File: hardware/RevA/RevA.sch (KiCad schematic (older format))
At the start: 143 parts, among them J1 USB_C_Receptacle_USB2.0, J2 DNP Conn_02x02_Odd_Even, J3 DNP Conn_01x02, J4 DNP Conn_02x03_Odd_Even, J5 DNP Conn_01x02, SW1 SW_Push, SW2 SW_Push, U1 SY8120B1ABC, U10 SPI RAM LY68L6400SLIT, U2 XC6206P25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

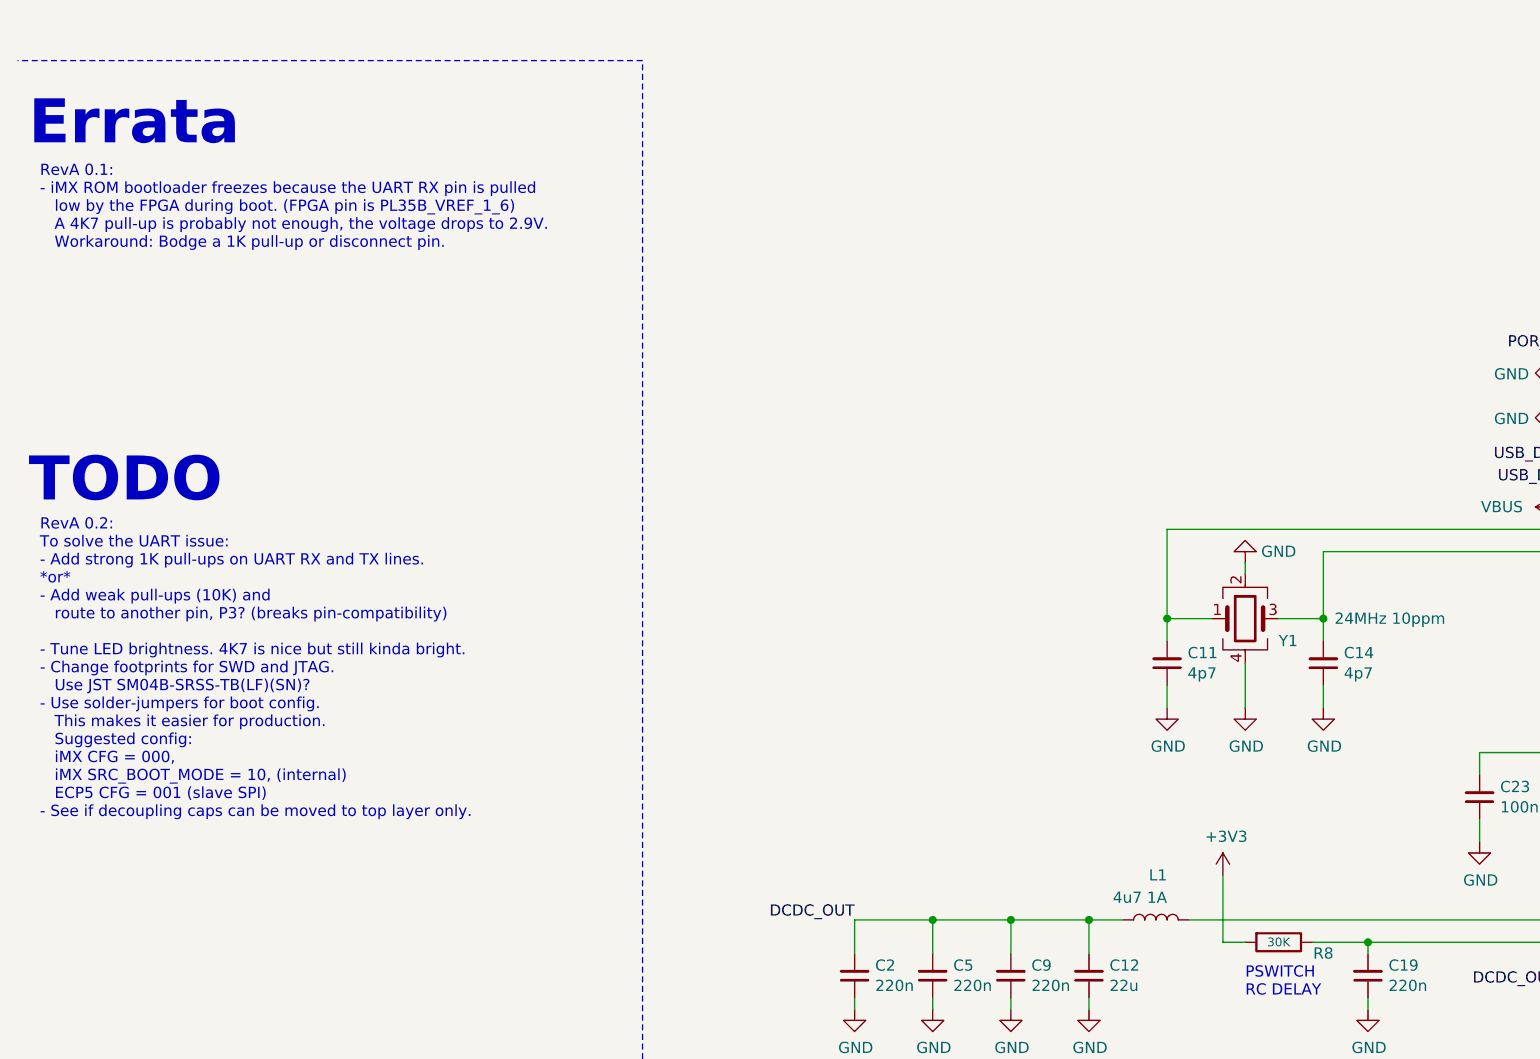
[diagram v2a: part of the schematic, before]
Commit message: Changed xtal load caps to 20pF
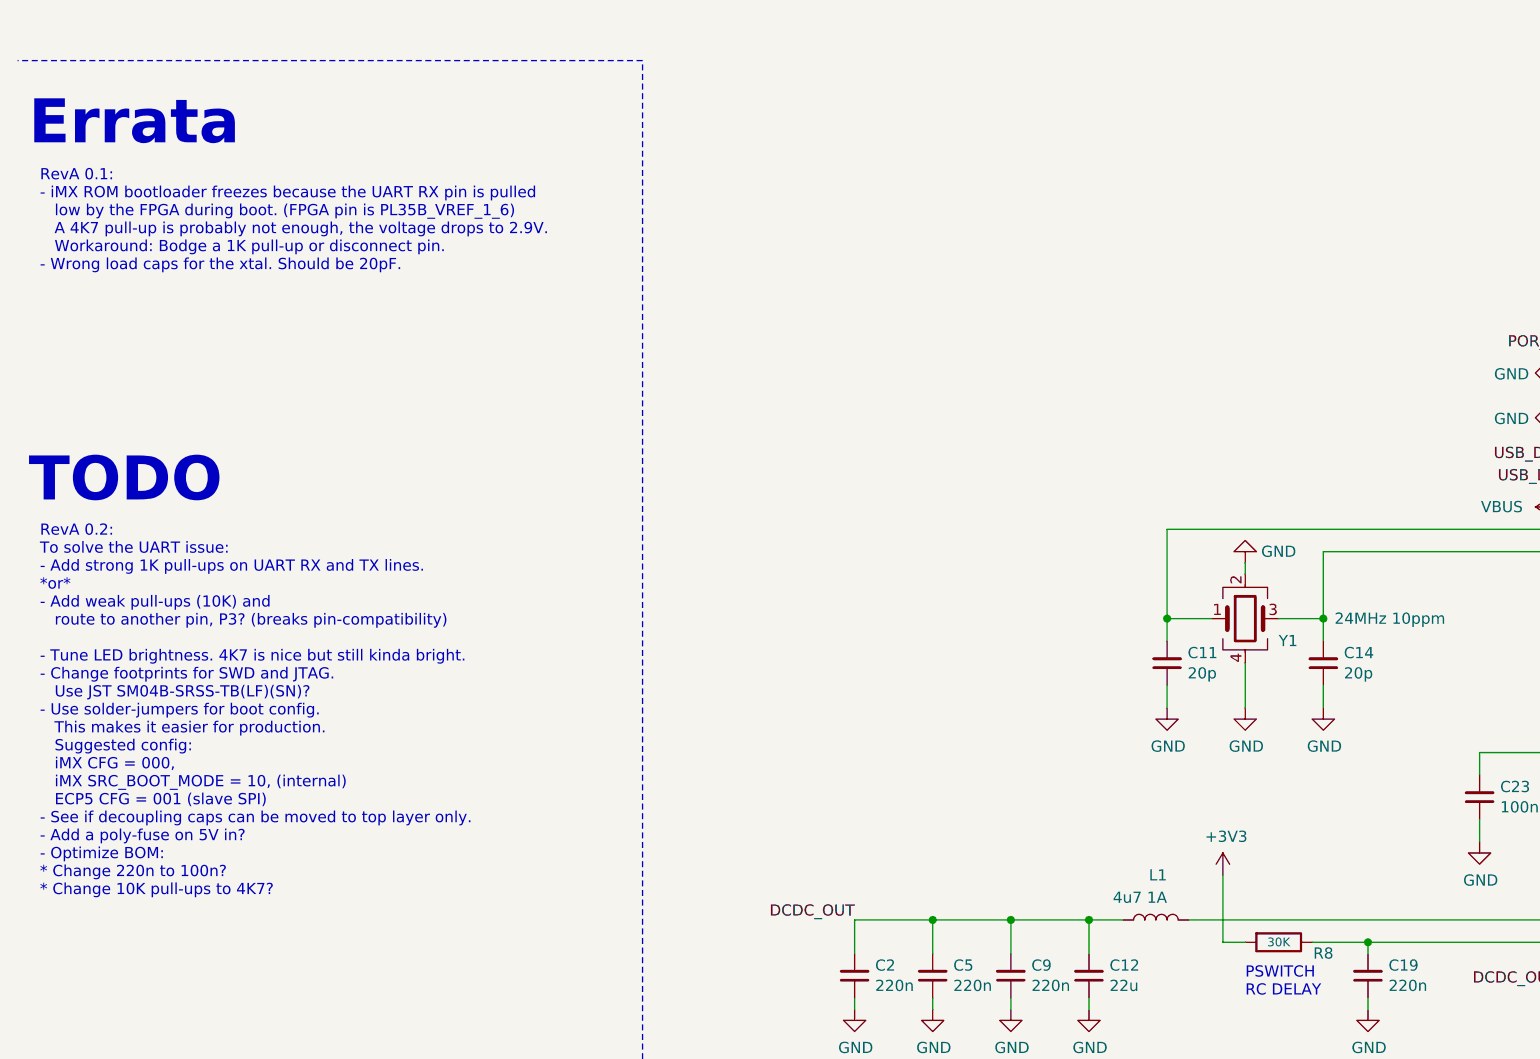
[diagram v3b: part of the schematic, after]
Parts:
- C11, C14: value 4p7 -> 20p
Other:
- note added: "RevA 0.1:\n- iMX ROM bootloader freezes because the UART RX pin is pulled\n low by the FPGA during boot. (FPGA pin is PL35B_VREF_1_6)\n A 4K7 pull-up is probably not enough, the voltage drops to 2.9V.\n Workaround: Bodge a 1K pull-up or disconnect pin.\n- Wrong load caps for the xtal. Should be 20pF."
- note removed: "RevA 0.1:\n- iMX ROM bootloader freezes because the UART RX pin is pulled\n low by the FPGA during boot. (FPGA pin is PL35B_VREF_1_6)\n A 4K7 pull-up is probably not enough, the voltage drops to 2.9V.\n Workaround: Bodge a 1K pull-up or disconnect pin.\n"
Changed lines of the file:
@@
 P 5700 12900
 F 0 "C11" H 5608 12854 50  0000 R CNN
-F 1 "4p7" H 5608 12945 50  0000 R CNN
+F 1 "20p" H 5608 12945 50  0000 R CNN
 F 2 "Capacitor_SMD:C_0402_1005Metric" H 5700 12900 50  0001 C CNN
 F 3 " " H 5700 12900 50  0001 C CNN
@@
 P 6400 12900
 F 0 "C14" H 6308 12854 50  0000 R CNN
-F 1 "4p7" H 6308 12945 50  0000 R CNN
+F 1 "20p" H 6308 12945 50  0000 R CNN
 F 2 "Capacitor_SMD:C_0402_1005Metric" H 6400 12900 50  0001 C CNN
 F 3 " " H 6400 12900 50  0001 C CNN
@@
 Text Notes 600  10600 0    197  ~ 39
 Errata
-Text Notes 650  11050 0    50   ~ 0
-RevA 0.1:\n- iMX ROM bootloader freezes because the UART RX pin is pulled\n   low by the FPGA during boot. (FPGA pin is PL35B_VREF_1_6)\n   A 4K7 pull-up is probably not enough, the voltage drops to 2.9V.\n   Workaround: Bodge a 1K pull-up or disconnect pin.\n
+Text Notes 650  11150 0    50   ~ 0
+RevA 0.1:\n- iMX ROM bootloader freezes because the UART RX pin is pulled\n   low by the FPGA during boot. (FPGA pin is PL35B_VREF_1_6)\n   A 4K7 pull-up is probably not enough, the voltage drops to 2.9V.\n   Workaround: Bodge a 1K pull-up or disconnect pin.\n- Wrong load caps for the xtal. Should be 20pF.
 Text Notes 600  12200 0    197  ~ 39
 TODO
-Text Notes 650  13600 0    50   ~ 0
-RevA 0.2:\nTo solve the UART issue:\n- Add strong 1K pull-ups on UART RX and TX lines.\n*or*\n- Add weak pull-ups (10K) and\n   route to another pin, P3? (breaks pin-compatibility)\n\n- Tune LED brightness. 4K7 is nice but still kinda bright.\n- Change footprints for SWD and JTAG.\n   Use JST SM04B-SRSS-TB(LF)(SN)?\n- Use solder-jumpers for boot config.\n   This makes it easier for production.\n   Suggested config:\n   iMX CFG = 000,\n   iMX SRC_BOOT_MODE = 10, (internal)\n   ECP5 CFG = 001 (slave SPI)\n- See if decoupling caps can be moved to top layer only.
+Text Notes 650  13950 0    50   ~ 0
+RevA 0.2:\nTo solve the UART issue:\n- Add strong 1K pull-ups on UART RX and TX lines.\n*or*\n- Add weak pull-ups (10K) and\n   route to another pin, P3? (breaks pin-compatibility)\n\n- Tune LED brightness. 4K7 is nice but still kinda bright.\n- Change footprints for SWD and JTAG.\n   Use JST SM04B-SRSS-TB(LF)(SN)?\n- Use solder-jumpers for boot config.\n   This makes it easier for production.\n   Suggested config:\n   iMX CFG = 000,\n   iMX SRC_BOOT_MODE = 10, (internal)\n   ECP5 CFG = 001 (slave SPI)\n- See if decoupling caps can be moved to top layer only.\n- Add a poly-fuse on 5V in?\n- Optimize BOM:\n* Change 220n to 100n?\n* Change 10K pull-ups to 4K7?
 $EndSCHEMATC

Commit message: RevA 0.2 updates
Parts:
- added R36, R37: 1K, Resistor_SMD:R_0402_1005Metric, symbol Device:R
- R20, R21, R22, R25, R26, R27, R28, R29, R30, R31, R32: value 4K7 -> 10K
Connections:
- net +3V3: now also R36.2, R37.2
- net ALT0_LPUART1_RXD: now also R36.1
- net ALT0_LPUART1_TXD: now also R37.1
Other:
- note added: "RevA 0.2:\n[X] Add strong 1K pull-ups on UART RX and TX lines.\n[X] Tune LED brightness. 10K looks good\n[ ] Fix incorrect RGB LED footprint, pin 1. Also R and G are swapped.\n[ ] Change footprints for SWD and JTAG.\n Use JST SM04B-SRSS-TB(LF)(SN)?\n[ ] Use solder-jumpers for boot config.\n This makes it easier for production.\n Suggested config:\n iMX CFG = 000,\n iMX SRC_BOOT_MODE = 10, (intern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"
- note removed: "RevA 0.2:\nTo solve the UART issue:\n- Add strong 1K pull-ups on UART RX and TX lines.\n*or*\n- Add weak pull-ups (10K) and\n route to another pin, P3? (breaks pin-compatibility)\n\n- Tune LED brightness. 4K7 is nice but still kinda bright.\n- Change footprints for SWD and JTAG.\n Use JST SM04B-SRSS-TB(LF)(SN)?\n- Use solder-jumpers for boot config.\n This makes it easier for production.\n Sugges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"
- moved on the sheet: TP1, TP2
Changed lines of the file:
@@
 Title "Pergola"
 Date "2019-11-16"
-Rev "A 0.2"
+Rev "A 0.2 (wip)"
 Comp "Konrad Beckmann"
 Comment1 "https://pergola.xil.se"
@@
 Wire Wire Line
 	14000 14050 14000 13950
-$Comp
-L Connector:TestPoint TP1
-U 1 1 5DFADC3C
-P 10050 11600
-F 0 "TP1" V 9950 12000 50  0000 C CNN
-F 1 "RX" V 10050 11850 50  0000 C CNN
-F 2 "TestPoint:TestPoint_Pad_D1.0mm" H 10250 11600 50  0001 C CNN
-F 3 " " H 10250 11600 50  0001 C CNN
-	1    10050 11600
-	0    -1   -1   0
-$EndComp
-Wire Wire Line
-	10050 11600 11000 11600
-$Comp
-L Connector:TestPoint TP2
-U 1 1 5E071D2E
-P 10050 11700
-F 0 "TP2" V 10150 12100 50  0000 C CNN
-F 1 "TX" V 10050 11950 50  0000 C CNN
-F 2 "TestPoint:TestPoint_Pad_D1.0mm" H 10250 11700 50  0001 C CNN
-F 3 " " H 10250 11700 50  0001 C CNN
-	1    10050 11700
-	0    -1   -1   0
-$EndComp
 Wire Wire Line
-	10050 11700 11000 11700
+	9600 11600 9650 11600
 Text Notes 13700 13400 0    50   ~ 0
 ECP5 CFGMDN[2:0]\n001: Slave SPI\n101: Slave Serial\n111: Slave Parallell (N/A)\n010: Master SPI\n\nNote: Use 4K7 for pull-up and <500R for pull-down\nDefault is internal pull-up.
@@
 P 9450 4050
 F 0 "R25" V 9400 3850 50  0000 C CNN
-F 1 "4K7" V 9450 4050 39  0000 C CNN
+F 1 "10K" V 9450 4050 39  0000 C CNN
 F 2 "Resistor_SMD:R_0402_1005Metric" V 9380 4050 50  0001 C CNN
 F 3 " " H 9450 4050 50  0001 C CNN
@@
 P 9450 4250
 F 0 "R26" V 9400 4050 50  0000 C CNN
-F 1 "4K7" V 9450 4250 39  0000 C CNN
+F 1 "10K" V 9450 4250 39  0000 C CNN
 F 2 "Resistor_SMD:R_0402_1005Metric" V 9380 4250 50  0001 C CNN
 F 3 " " H 9450 4250 50  0001 C CNN
@@
 P 9450 4450
 F 0 "R27" V 9400 4250 50  0000 C CNN
-F 1 "4K7" V 9450 4450 39  0000 C CNN
+F 1 "10K" V 9450 4450 39  0000 C CNN
 F 2 "Resistor_SMD:R_0402_1005Metric" V 9380 4450 50  0001 C CNN
 F 3 " " H 9450 4450 50  0001 C CNN
@@
 P 9450 4650
 F 0 "R28" V 9400 4450 50  0000 C CNN
-F 1 "4K7" V 9450 4650 39  0000 C CNN
+F 1 "10K" V 9450 4650 39  0000 C CNN
 F 2 "Resistor_SMD:R_0402_1005Metric" V 9380 4650 50  0001 C CNN
 F 3 " " H 9450 4650 50  0001 C CNN
@@
 P 9450 4850
 F 0 "R29" V 9400 4650 50  0000 C CNN
-F 1 "4K7" V 9450 4850 39  0000 C CNN
+F 1 "10K" V 9450 4850 39  0000 C CNN
 F 2 "Resistor_SMD:R_0402_1005Metric" V 9380 4850 50  0001 C CNN
 F 3 " " H 9450 4850 50  0001 C CNN
@@
 P 9450 5050
 F 0 "R30" V 9400 4850 50  0000 C CNN
-F 1 "4K7" V 9450 5050 39  0000 C CNN
+F 1 "10K" V 9450 5050 39  0000 C CNN
 F 2 "Resistor_SMD:R_0402_1005Metric" V 9380 5050 50  0001 C CNN
 F 3 " " H 9450 5050 50  0001 C CNN
@@
 P 9450 5250
 F 0 "R31" V 9400 5050 50  0000 C CNN
-F 1 "4K7" V 9450 5250 39  0000 C CNN
+F 1 "10K" V 9450 5250 39  0000 C CNN
 F 2 "Resistor_SMD:R_0402_1005Metric" V 9380 5250 50  0001 C CNN
 F 3 " " H 9450 5250 50  0001 C CNN
@@
 P 9450 5450
 F 0 "R32" V 9400 5250 50  0000 C CNN
-F 1 "4K7" V 9450 5450 39  0000 C CNN
+F 1 "10K" V 9450 5450 39  0000 C CNN
 F 2 "Resistor_SMD:R_0402_1005Metric" V 9380 5450 50  0001 C CNN
 F 3 " " H 9450 5450 50  0001 C CNN
@@
 P 11100 4350
 F 0 "R20" V 11050 4150 50  0000 C CNN
-F 1 "4K7" V 11100 4350 39  0000 C CNN
+F 1 "10K" V 11100 4350 39  0000 C CNN
 F 2 "Resistor_SMD:R_0402_1005Metric" V 11030 4350 50  0001 C CNN
 F 3 " " H 11100 4350 50  0001 C CNN
@@
 P 11100 4550
 F 0 "R21" V 11050 4350 50  0000 C CNN
-F 1 "4K7" V 11100 4550 39  0000 C CNN
+F 1 "10K" V 11100 4550 39  0000 C CNN
 F 2 "Resistor_SMD:R_0402_1005Metric" V 11030 4550 50  0001 C CNN
 F 3 " " H 11100 4550 50  0001 C CNN
@@
 P 11100 4750
 F 0 "R22" V 11050 4550 50  0000 C CNN
-F 1 "4K7" V 11100 4750 39  0000 C CNN
+F 1 "10K" V 11100 4750 39  0000 C CNN
 F 2 "Resistor_SMD:R_0402_1005Metric" V 11030 4750 50  0001 C CNN
 F 3 " " H 11100 4750 50  0001 C CNN
@@
 TODO
 Text Notes 650  13950 0    50   ~ 0
-RevA 0.2:\nTo solve the UART issue:\n- Add strong 1K pull-ups on UART RX and TX lines.\n*or*\n- Add weak pull-ups (10K) and\n   route to another pin, P3? (breaks pin-compatibility)\n\n- Tune LED brightness. 4K7 is nice but still kinda bright.\n- Change footprints for SWD and JTAG.\n   Use JST SM04B-SRSS-TB(LF)(SN)?\n- Use solder-jumpers for boot config.\n   This makes it easier for production.\n   Suggested config:\n   iMX CFG = 000,\n   iMX SRC_BOOT_MODE = 10, (internal)\n   ECP5 CFG = 001 (slave SPI)\n- See if decoupling caps can be moved to top layer only.\n- Add a poly-fuse on 5V in?\n- Optimize BOM:\n* Change 220n to 100n?\n* Change 10K pull-ups to 4K7?
+RevA 0.2:\n[X] Add strong 1K pull-ups on UART RX and TX lines.\n[X] Tune LED brightness. 10K looks good\n[ ] Fix incorrect RGB LED footprint, pin 1. Also R and G are swapped.\n[ ] Change footprints for SWD and JTAG.\n   Use JST SM04B-SRSS-TB(LF)(SN)?\n[ ] Use solder-jumpers for boot config.\n   This makes it easier for production.\n   Suggested config:\n   iMX CFG = 000,\n   iMX SRC_BOOT_MODE = 10, (internal)\n   ECP5 CFG = 001 (slave SPI)\n[ ] See if decoupling caps can be moved to top layer only.\n[ ] Update Rev A 0.2 text\n[ ] Move the iMX so it's centered instead aligned usb pins?\n[ ] Add a poly-fuse on 5V in?\n\nOptimize BOM:\n[ ] Change 220n to 100n?
+$Comp
+L Connector:TestPoint TP2
+U 1 1 5E071D2E
+P 9600 11700
+F 0 "TP2" V 9600 12100 50  0000 C CNN
+F 1 "TX" V 9600 11950 50  0000 C CNN
+F 2 "TestPoint:TestPoint_Pad_D1.0mm" H 9800 11700 50  0001 C CNN
+F 3 " " H 9800 11700 50  0001 C CNN
+	1    9600 11700
+	0    -1   -1   0
+$EndComp
+$Comp
+L Connector:TestPoint TP1
+U 1 1 5DFADC3C
+P 9600 11600
+F 0 "TP1" V 9600 12000 50  0000 C CNN
+F 1 "RX" V 9600 11850 50  0000 C CNN
+F 2 "TestPoint:TestPoint_Pad_D1.0mm" H 9800 11600 50  0001 C CNN
+F 3 " " H 9800 11600 50  0001 C CNN
+	1    9600 11600
+	0    -1   -1   0
+$EndComp
+$Comp
+L Device:R R36
+U 1 1 5E18C3EE
+P 9650 11350
+F 0 "R36" H 9700 11200 50  0000 C CNN
+F 1 "1K" V 9650 11350 39  0000 C CNN
+F 2 "Resistor_SMD:R_0402_1005Metric" V 9580 11350 50  0001 C CNN
+F 3 " " H 9650 11350 50  0001 C CNN
+	1    9650 11350
+	-1   0    0    1
+$EndComp
+$Comp
+L Device:R R37
+U 1 1 5E18CBE6
+P 9750 11350
+F 0 "R37" H 9700 11200 50  0000 C CNN
+F 1 "1K" V 9750 11350 39  0000 C CNN
+F 2 "Resistor_SMD:R_0402_1005Metric" V 9680 11350 50  0001 C CNN
+F 3 " " H 9750 11350 50  0001 C CNN
+	1    9750 11350
+	-1   0    0    1
+$EndComp
+Wire Wire Line
+	9750 11500 9750 11700
+Connection ~ 9750 11700
+Wire Wire Line
+	9750 11700 11000 11700
+Wire Wire Line
+	9600 11700 9750 11700
+Wire Wire Line
+	9650 11500 9650 11600
+Connection ~ 9650 11600
+Wire Wire Line
+	9650 11600 11000 11600
+$Comp
+L power:+3V3 #PWR0137
+U 1 1 5E3BA75C
+P 9650 11000
+F 0 "#PWR0137" H 9650 10850 50  0001 C CNN
+F 1 "+3V3" H 9665 11173 50  0000 C CNN
+F 2 "" H 9650 11000 50  0001 C CNN
+F 3 "" H 9650 11000 50  0001 C CNN
+	1    9650 11000
+	1    0    0    -1
+$EndComp
+Wire Wire Line
+	9650 11000 9650 11100
+Wire Wire Line
+	9650 11100 9750 11100
+Wire Wire Line
+	9750 11100 9750 11200
+Connection ~ 9650 11100
+Wire Wire Line
+	9650 11100 9650 11200
 $EndSCHEMATC
